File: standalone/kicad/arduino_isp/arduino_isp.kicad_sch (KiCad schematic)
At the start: 10 parts, among them J1 ICSP, J2 ICSP, J3 Conn_01x09, J4 Conn_01x06

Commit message: Atualizações na placa
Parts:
- removed J2: ICSP, Connector_IDC:IDC-Header_2x03_P2.54mm_Vertical, symbol Connector_Generic:Conn_02x03_Odd_Even

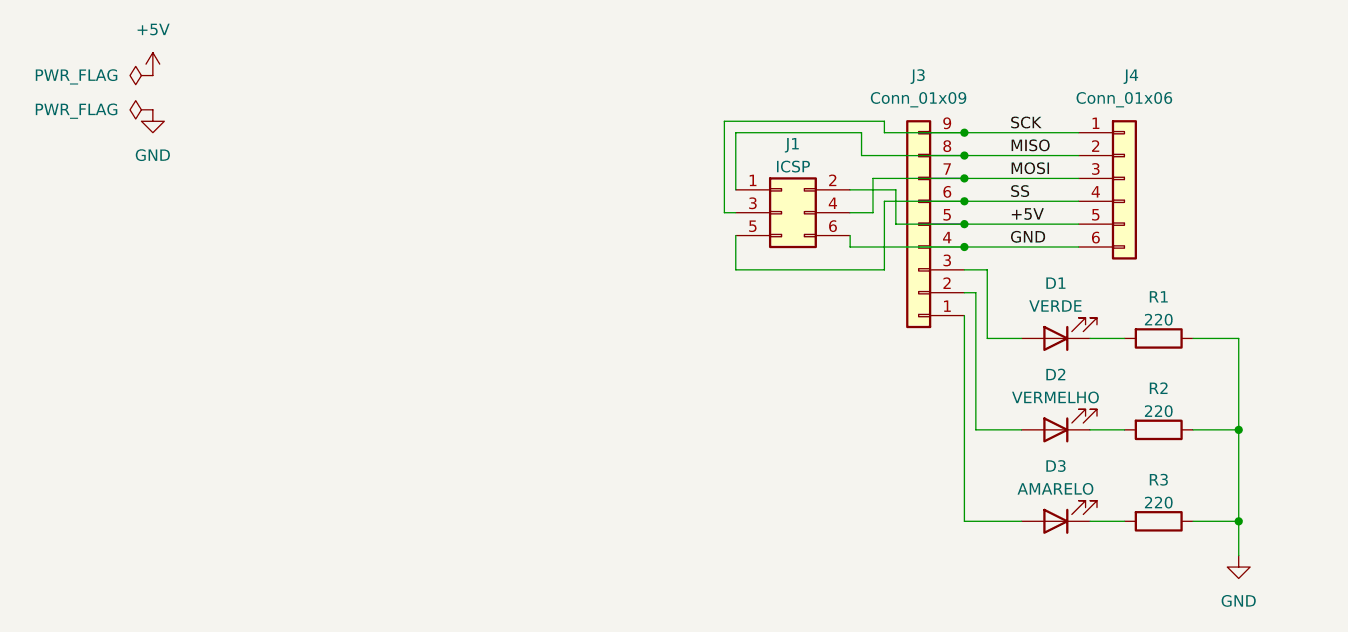
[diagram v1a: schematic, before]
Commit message: Troca do conector de 9 para 10 pinos
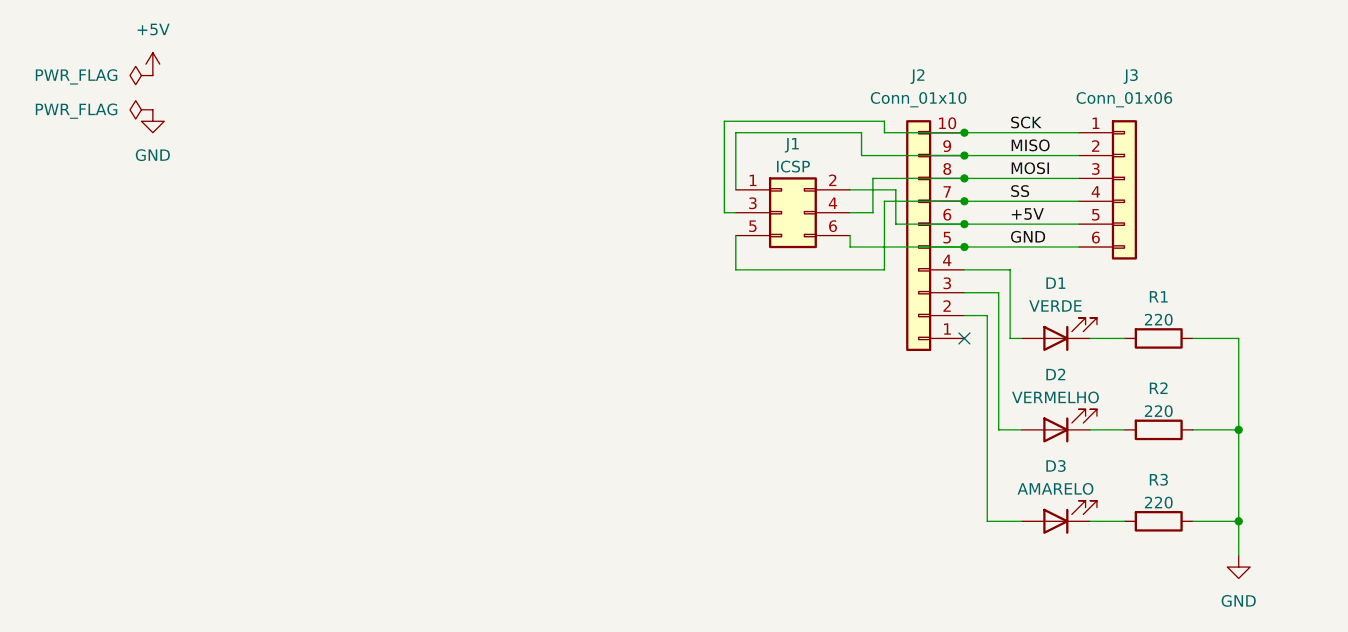
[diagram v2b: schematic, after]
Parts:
- removed J3: Conn_01x09, Connector_PinSocket_2.54mm:PinSocket_1x09_P2.54mm_Vertical, symbol Connector_Generic:Conn_01x09
- added J2: Conn_01x10, Connector_PinSocket_2.54mm:PinSocket_1x10_P2.54mm_Vertical, symbol Connector_Generic:Conn_01x10
- renumbered J4 to J3
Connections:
- net +5V: now also J2.6 (Pin_6)
- net GND: now also J2.5 (Pin_5)
- net MISO: now also J2.9 (Pin_9)
- net MOSI: now also J2.8 (Pin_8)
- net SCK: now also J2.10 (Pin_10)
- net SS: now also J2.7 (Pin_7)
- net at D2.2 (A): now also J2.3 (Pin_3)
- net at D3.2 (A): now also J2.2 (Pin_2)
- net at D1.2 (A): now also J2.4 (Pin_4)
- no-connect marks 0 -> 1

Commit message: Finalização da placa Aruino ISP
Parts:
- removed J1: ICSP, Connector_IDC:IDC-Header_2x03_P2.54mm_Vertical, symbol Connector_Generic:Conn_02x03_Odd_Even
- renumbered J2 to J1, J3 to J2
